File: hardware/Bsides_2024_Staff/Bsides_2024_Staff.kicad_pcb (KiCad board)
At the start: 2 copper layers, 129.4 x 129.4 mm, 43 parts, among them J1 Battery, J2 Battery, J3 OLED, J4 Add_On, P1 USB_C_Plug_USB2.0, Q1 DMG3415U-7, SW1 ON, SW2 RESET, SW3 BOOT, SW4 RESET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

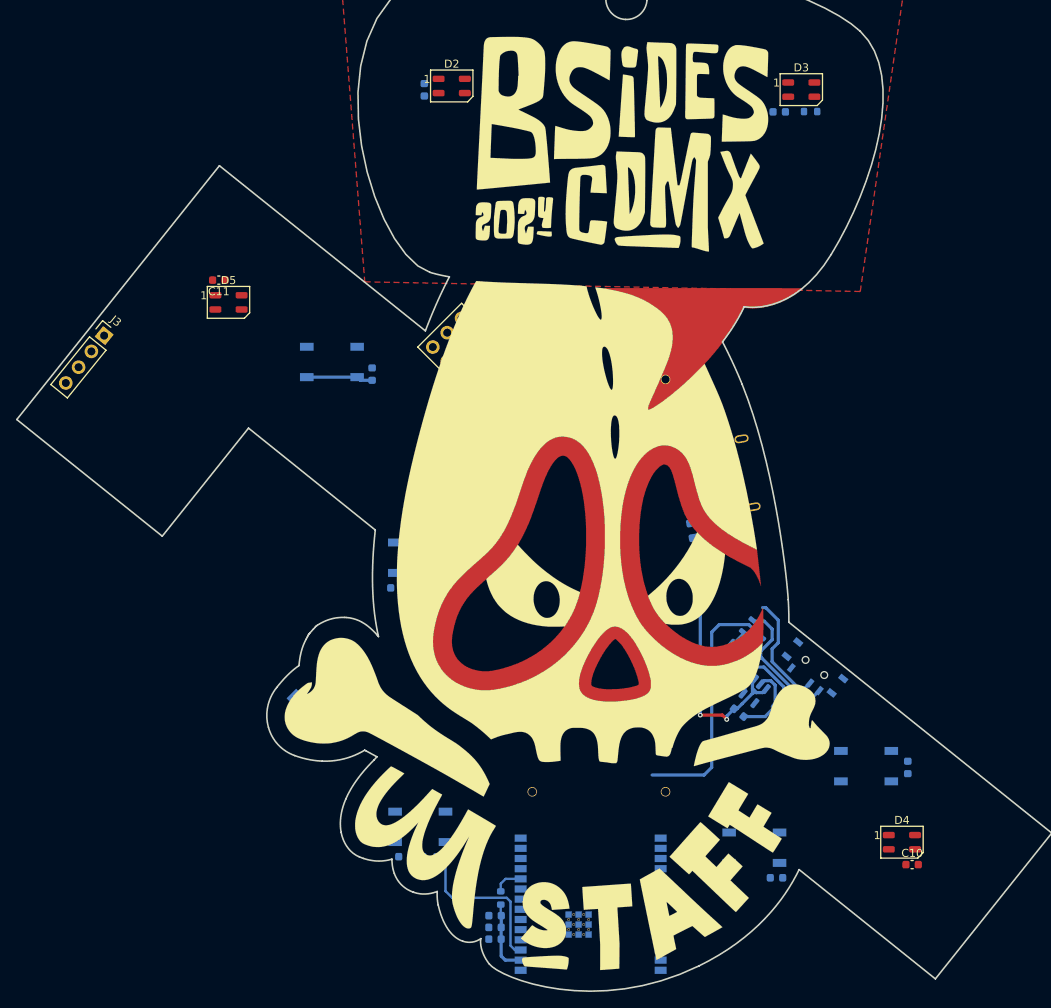
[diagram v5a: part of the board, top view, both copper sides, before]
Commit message: feat(Hw):Update_Staff_Sch_And_PCB
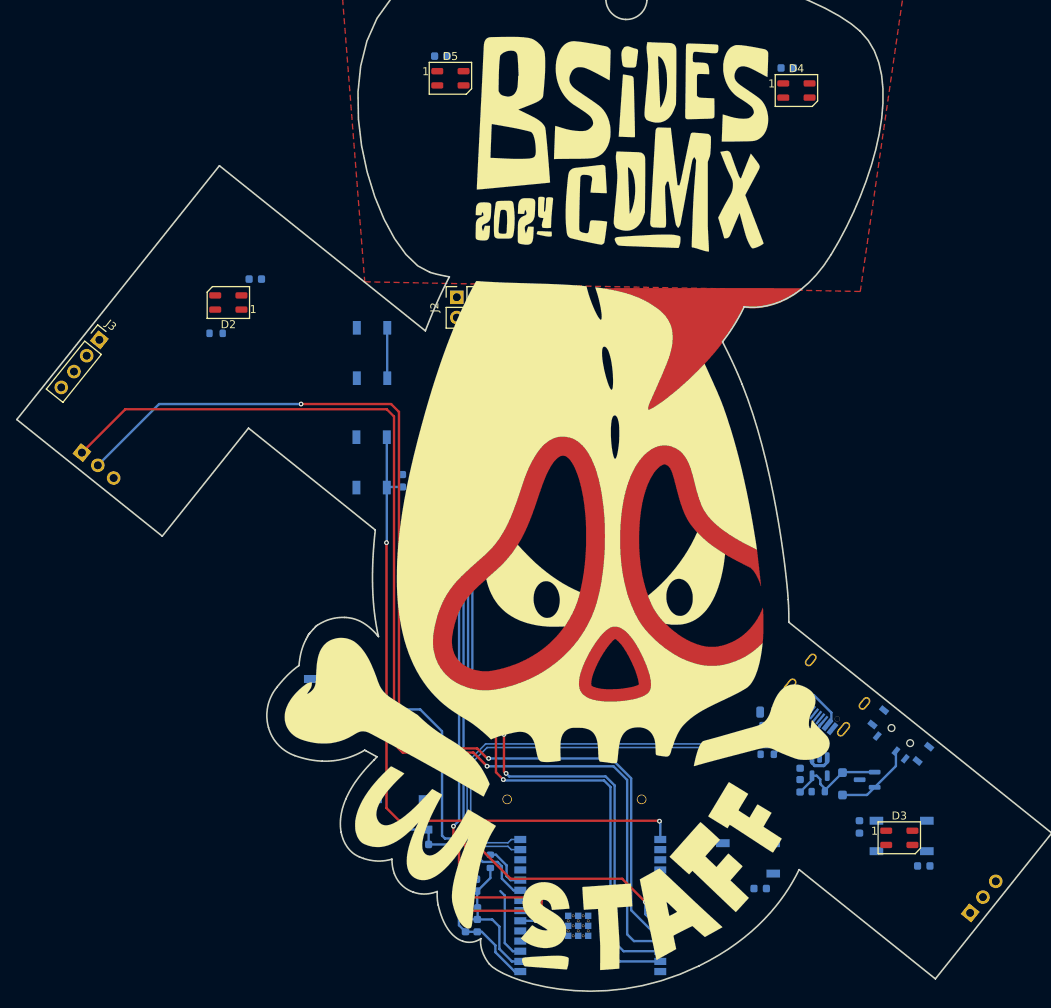
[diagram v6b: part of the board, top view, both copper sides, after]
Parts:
- removed R7: 470, Resistor_SMD:R_0603_1608Metric
- added J5: Battery, bsides:BH-AA-A1AJ020, B.Cu at (140.1, 100.3)
- added J6: Battery, bsides:BH-AA-A1AJ020, B.Cu at (156.9, 100.3)
- added R6: 470, Resistor_SMD:R_0603_1608Metric, B.Cu at (103.7, 67.8)
- C1: value 10uF -> 1uF
- C10, C11: moved to B.Cu
- C13: value 1uF -> 0.1uF
- C14, C15: value 10uF -> 0.1uF
- C3, C4, C5: value 0.1uF -> 10uF
- J1: value Battery -> Serial_IN; footprint bsides:BH-AA-A1AJ020 -> Connector_PinHeader_2.54mm:PinHeader_1x03_P2.54mm_Vertical
- J2: value Battery -> Add_On; footprint bsides:BH-AA-A1AJ020 -> Connector_PinSocket_2.54mm:PinSocket_2x03_P2.54mm_Vertical; moved to F.Cu
- J4: value Add_On -> Serial_OUT; footprint Connector_PinSocket_2.54mm:PinSocket_2x03_P2.54mm_Vertical -> Connector_PinSocket_2.54mm:PinSocket_1x03_P2.54mm_Vertical; moved to B.Cu
- U1: value ESP32-C6-WROOM-1U-N4 -> ESP32-C6-WROOM-1-N4
- moved C15 110.6 mm to (131.8, 33.2)
- moved C10 100.8 mm to (175.1, 34.6), turned to 180 degrees
- moved J4 95.3 mm to (197.9, 140.3), turned to -39 degrees
- moved D4 94.9 mm to (176.2, 37.5)
- moved D3 94.3 mm to (189.1, 130.9)
- moved C9 89.9 mm to (184.1, 129.5), turned to -90 degrees
- moved SW7 81.0 mm to (170.2, 133.4)
- moved C12 80.5 mm to (115.9, 116.7), turned to 180 degrees
- moved C11 75.0 mm to (129.5, 131.7), turned to 0 degrees
- moved SW6 74.6 mm to (189.4, 130.7), turned to 180 degrees
- moved C6 72.6 mm to (127.0, 86.2), turned to -90 degrees
- moved SW3 67.9 mm to (123.1, 84.0), turned to -90 degrees
- moved SW5 66.9 mm to (118.7, 112.9), turned to 180 degrees
- moved SW2 59.5 mm to (123.2, 70.3), turned to -90 degrees
- moved J1 58.7 mm to (86.9, 82.7), turned to -128.699 degrees
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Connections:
- C1 pad 1: VBUS -> /VOUT
- C11 pad 2: /VOUT -> /GPIO1
- C12 pad 2: /VOUT -> /GPIO15
- C13 pad 1: /VOUT -> GND
- C13 pad 2: GND -> /GPIO22
- C14 pad 1: /VOUT -> GND
- C14 pad 2: GND -> /GPIO23
- C15 pad 1: /VOUT -> GND
- C15 pad 2: GND -> /VOUT
- C2 pad 1: Net-(D1-A) -> /VOUT
- C3 pad 1: GND -> /VOUT
- C3 pad 2: /BOOT -> GND
- C4 pad 1: GND -> VBUS
- C4 pad 2: /EN -> GND
- C5 pad 1: GND -> Net-(D1-A)
- C5 pad 2: /GPIO1 -> GND
- C6 pad 2: /GPIO22 -> /BOOT
- C7 pad 2: /GPIO15 -> /EN
- C8 pad 2: /GPIO23 -> /VOUT
- D2 pad 2: unconnected-(D2-DOUT-Pad2) -> Net-(D2-DOUT)
- D3 pad 4: Net-(D3-DIN) -> Net-(D2-DOUT)
- D5 pad 2: Net-(D2-DIN) -> unconnected-(D5-DOUT-Pad2)
- J1 pad 1: GND -> /GPIO16
- J1 pad 2: Net-(J1-Pin_2) -> /GPIO17
- J2 pad 1: Net-(J1-Pin_2) -> /VOUT
- J2 pad 2: +BATT -> GND
- J3 pad 1: /VOUT -> /SDA
- J3 pad 2: GND -> /SCL
- J3 pad 3: /SCL -> /VOUT
- J3 pad 4: /SDA -> GND
- J4 pad 1: /VOUT -> /GPIO4
- J4 pad 2: GND -> /GPIO5
- J4 pad 3: /SDA -> GND
- R1 pad 1: /PIN -> Net-(U1-IO8)
- SW1 pad 2: /VOUT -> Net-(D1-K)
- SW1 pad 3: Net-(D1-K) -> /VOUT
- SW5 pad 2: /GPIO22 -> /GPIO15
- SW6 pad 2: /GPIO15 -> /GPIO22
- U1 pad 10: /PIN -> Net-(U1-IO8)
- U1 pad 11: unconnected-(U1-IO10-Pad11) -> /PIN
- U1 pad 24: /RX -> /GPIO17
- U1 pad 25: /TX -> /GPIO16
- U1 pad 26: unconnected-(U1-IO3-Pad26) -> /GPIO3
- U1 pad 27: unconnected-(U1-IO2-Pad27) -> /GPIO2
- U1 pad 4: unconnected-(U1-IO4-Pad4) -> /GPIO4
- U1 pad 5: unconnected-(U1-IO5-Pad5) -> /GPIO5
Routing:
- net /GPIO16: track 0.00 -> 137.3 mm, vias 0 -> 1
- net /GPIO17: track 0.00 -> 134.4 mm, vias 0 -> 2
- net /GPIO3: track 0.00 -> 103.6 mm, vias 0 -> 2
- net /GPIO2: track 0.00 -> 102.2 mm, vias 0 -> 2
- net /SDA: track 0.00 -> 91.0 mm, vias 0 -> 2
- net /SCL: track 0.00 -> 86.8 mm, vias 0 -> 2
- net /BOOT: track 0.00 -> 85.5 mm, vias 0 -> 2
- net /GPIO15: track 0.00 -> 65.2 mm, vias 0 -> 2
- net /D-: track 0.00 -> 62.9 mm
- net /D+: track 0.00 -> 60.6 mm
- net +BATT: track 31.9 -> 0.00 mm
- net VBUS: track 35.3 -> 5.06 mm, vias 2 -> 0
- net /GPIO1: track 0.00 -> 23.1 mm
- net Net-(D1-K): track 20.6 -> 10.0 mm
- net /GPIO23: track 8.33 -> 0.00 mm
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
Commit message: feat(Hw):First_Route_Staff
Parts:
- J1: footprint Connector_PinHeader_2.54mm:PinHeader_1x03_P2.54mm_Vertical -> Connector_PinSocket_2.54mm:PinSocket_1x03_P2.54mm_Vertical
- J4: footprint Connector_PinSocket_2.54mm:PinSocket_1x03_P2.54mm_Vertical -> Connector_PinHeader_2.54mm:PinHeader_1x03_P2.54mm_Vertical; moved to F.Cu
- moved C13 8.30 mm to (183.8, 134.3), turned to 90 degrees
- moved R1 3.17 mm to (138.0, 137.0)
- moved C6 2.97 mm to (124.0, 86.3), turned to 0 degrees
- moved SW3 2.39 mm to (121.2, 82.5), turned to 180 degrees
- moved C14 1.23 mm to (172.9, 137.2), turned to 180 degrees
- moved SW2 0.72 mm to (123.2, 71.0), turned to 0 degrees
- moved C1 0.62 mm to (135.6, 139.0)
- moved C2 0.59 mm to (136.3, 141.3)
- moved C3 0.57 mm to (134.8, 141.3)
- moved D1 0.19 mm to (182.0, 123.9)
- turned J4 to 141.6 degrees
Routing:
- net /VOUT: track 17.9 -> 367.9 mm, vias 0 -> 8
- net Net-(D2-DOUT): track 0.00 -> 144.8 mm
- net Net-(D3-DOUT): track 0.00 -> 138.6 mm, vias 0 -> 2
- net /PIN: track 0.00 -> 103.0 mm, vias 0 -> 2
- net /EN: track 17.6 -> 107.2 mm, vias 0 -> 5
- net GND: track 17.3 -> 106.3 mm, vias 0 -> 7
- net /GPIO5: track 0.00 -> 73.5 mm, vias 0 -> 1
- net /GPIO4: track 0.00 -> 71.7 mm, vias 0 -> 1
- net +BATT: track 0.00 -> 57.4 mm, vias 0 -> 2
- net /SDA: track 91.0 -> 144.4 mm
- net /SCL: track 86.8 -> 135.1 mm
- net Net-(D4-DOUT): track 0.00 -> 41.3 mm
- net /GPIO22: track 0.00 -> 35.3 mm
- net /GPIO23: track 0.00 -> 22.2 mm
- net Net-(J5-Pin_1): track 0.00 -> 16.8 mm
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- added copper zone on B.Cu, net GND

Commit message: feat(Hw):Moved_Buttons_sponsor
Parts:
- moved C12 78.5 mm to (192.8, 132.0)
- moved SW5 78.5 mm to (195.6, 128.3)
- moved C13 20.3 mm to (164.0, 130.2)
- moved SW6 20.3 mm to (169.5, 126.6)
- moved C14 11.7 mm to (161.4, 139.5), turned to 90 degrees
- moved J1 4.96 mm to (90.7, 85.9), turned to 51.301 degrees
- moved SW7 4.74 mm to (166.5, 136.4)
- moved C9 0.55 mm to (184.0, 129.0)
- moved C5 0.39 mm to (176.7, 124.0)
- moved C4 0.38 mm to (176.7, 121.0)
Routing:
- net GND: track 106.3 -> 134.6 mm, vias 7 -> 12
- net /GPIO15: track 69.1 -> 47.6 mm, vias 2 -> 0
- net /GPIO22: track 35.3 -> 20.3 mm
- net /GPIO23: track 22.2 -> 10.6 mm
- net /VOUT: track 367.9 -> 373.7 mm
- net +BATT: track 57.4 -> 59.4 mm
- net /GPIO16: track 136.6 -> 138.2 mm
